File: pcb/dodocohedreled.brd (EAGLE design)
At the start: 50 x 47.5 mm, 11 parts

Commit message: Update for RevC
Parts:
- U$2, U$3, U$4, U$5, U$6: value D_EDGE -> D_EDGESLOT; device dodocohedreled:D_EDGE -> dodocohedreled:D_EDGE_SLOT
- moved C2 0.90 mm to (-1.60, 19.1)
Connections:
- net 5V: now also U$2.P$7, U$2.P$9, U$3.P$7, U$3.P$9, U$4.P$7, U$4.P$9, U$5.P$7, U$5.P$9, U$6.P$7, U$6.P$9
- net DATA: now also U$2.P$8, U$3.P$8, U$4.P$8, U$5.P$8, U$6.P$8
- net GND: now also U$2.P$10, U$2.P$6, U$3.P$10, U$3.P$6, U$4.P$10, U$4.P$6, U$5.P$10, U$5.P$6, U$6.P$10, U$6.P$6
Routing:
- net GND: track 109.7 -> 130.3 mm, vias 14 -> 19
- net N$10: track 7.30 -> 2.73 mm, vias 1 -> 0
- net 5V: track 12.3 -> 13.8 mm
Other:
- board size 50 x 47.5 mm -> 49.8 x 47.4 mm
- board text added: "BlinkyTile Rev. C"
- board text removed: "BlinkyTile Rev. B"

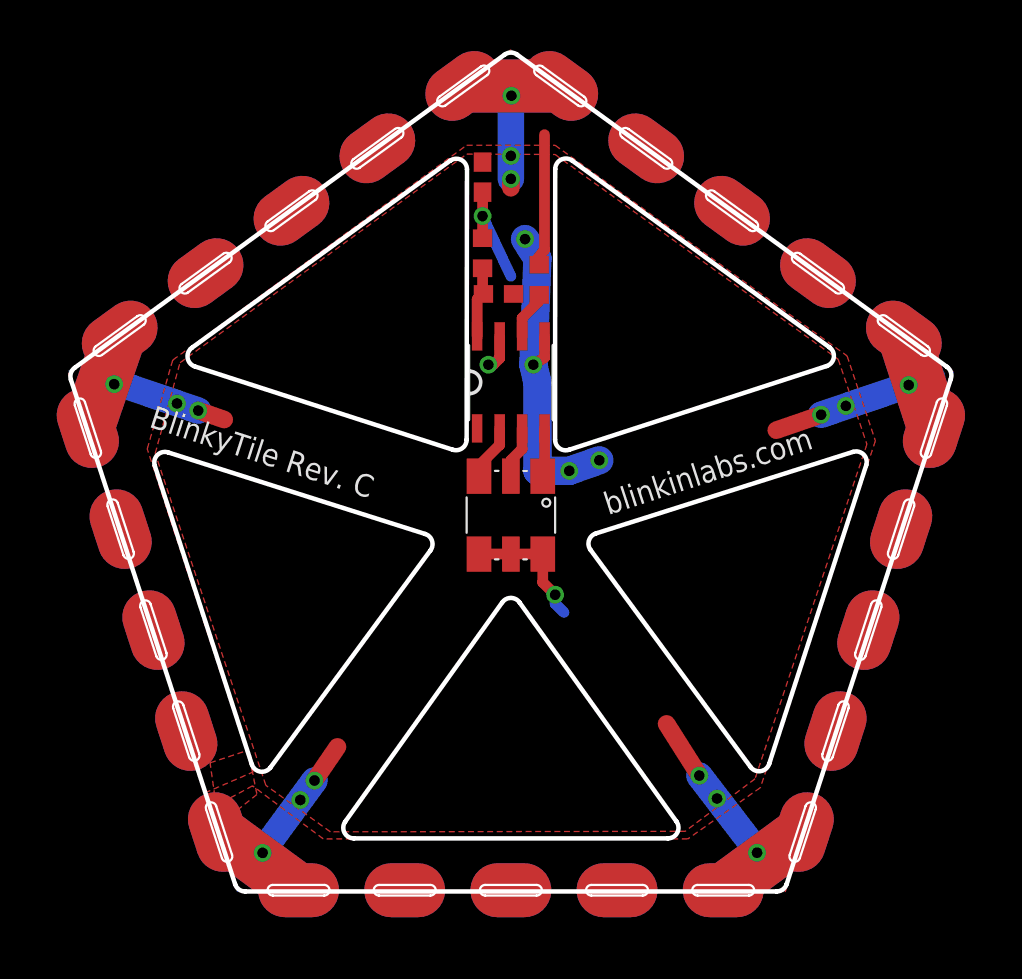
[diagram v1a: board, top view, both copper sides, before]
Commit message: Switch to WS2822S module, bump to RevD.
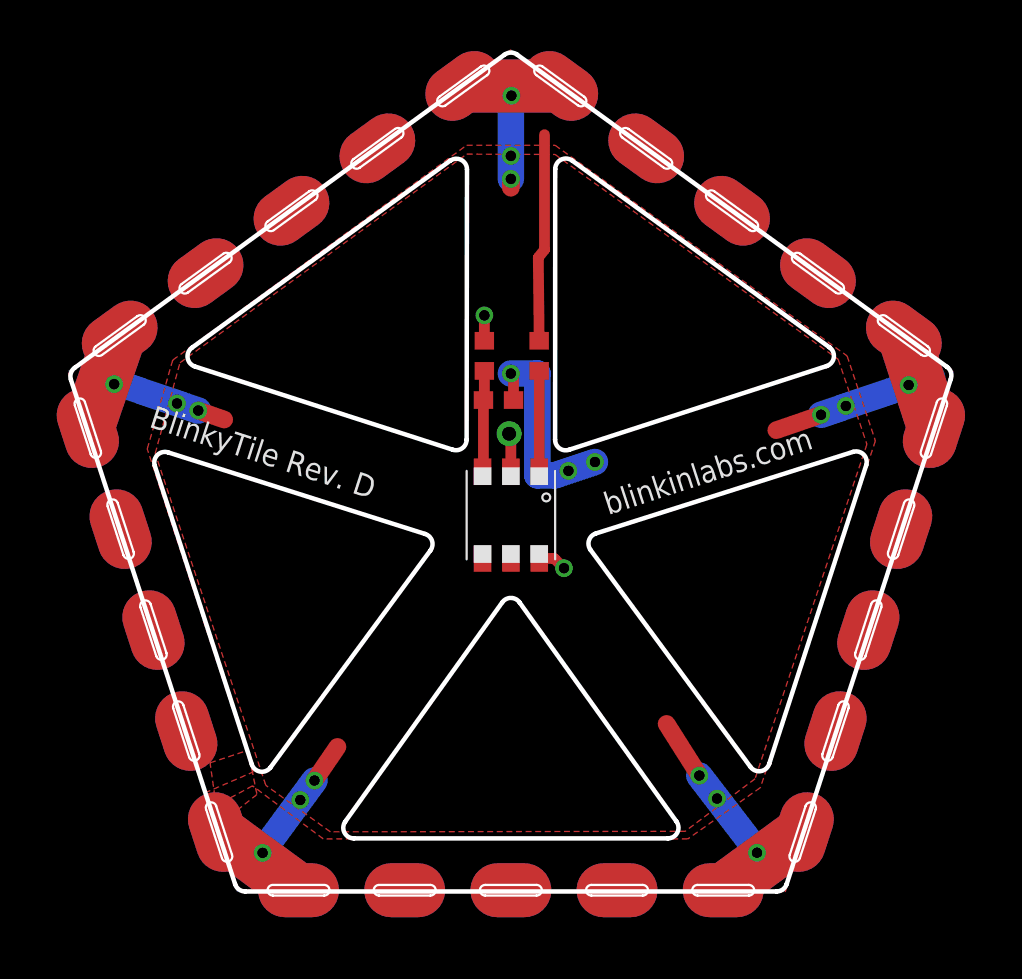
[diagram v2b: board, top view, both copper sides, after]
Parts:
- removed C2: 1uF, adafruit:C0603
- removed LED1: LED-TRICOLOR-5050", blinkinlabs:LED-TRICOLOR-5050-FIXED
- removed U$1: WS2821A, dodocohedreled:SOP8
- added U$7: WS2822S_LED, blinkinlabs:WS2822S_LED
- R1: value 10 -> 75
- R2: value 1k -> 10k
- moved C1 6.00 mm to (-0.70, 6.50)
- moved R1 5.80 mm to (-1.50, 9.00), turned to 270 degrees
- moved R2 4.30 mm to (1.60, 9.00)
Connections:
- removed net ADDR: U$1.7
- removed net N$10: R2.1, U$1.6
- removed net N$3: LED1.2, U$1.3
- removed net N$6: C1.1, R1.1, U$1.8
- new net ADRI: U$7.2
- net 5V: now also R1.1, U$7.6; no longer C2.1, LED1.4, LED1.5, LED1.6, R1.2
- net GND: now also U$7.4; no longer C2.2, U$1.5
- net N$1: now also C1.1, R1.2, U$7.3; no longer LED1.3, U$1.2
- net N$2: now also R2.1, U$7.1; no longer LED1.1, U$1.4
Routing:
- net 5V: track 13.8 -> 3.07 mm
- net GND: track 130.3 -> 123.6 mm, vias 19 -> 18
- net DATA: track 7.47 -> 11.8 mm
- net N$6: track 4.02 -> 0.00 mm
- net N$3: track 2.96 -> 0.00 mm
- net N$2: track 2.74 -> 5.70 mm
- net N$10: track 2.73 -> 0.00 mm
- net N$1: track 3.18 -> 5.74 mm
- net ADRI: track 0.00 -> 2.19 mm, vias 0 -> 1
- net ADDR: track 2.02 -> 0.00 mm, vias 1 -> 0
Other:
- board text added: "BlinkyTile Rev. D"
- board text removed: "BlinkyTile Rev. C"
